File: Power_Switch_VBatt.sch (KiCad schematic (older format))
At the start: 12 parts, among them P5 XT60, Q3 BC817-40, Q4 IPD90P03P4L

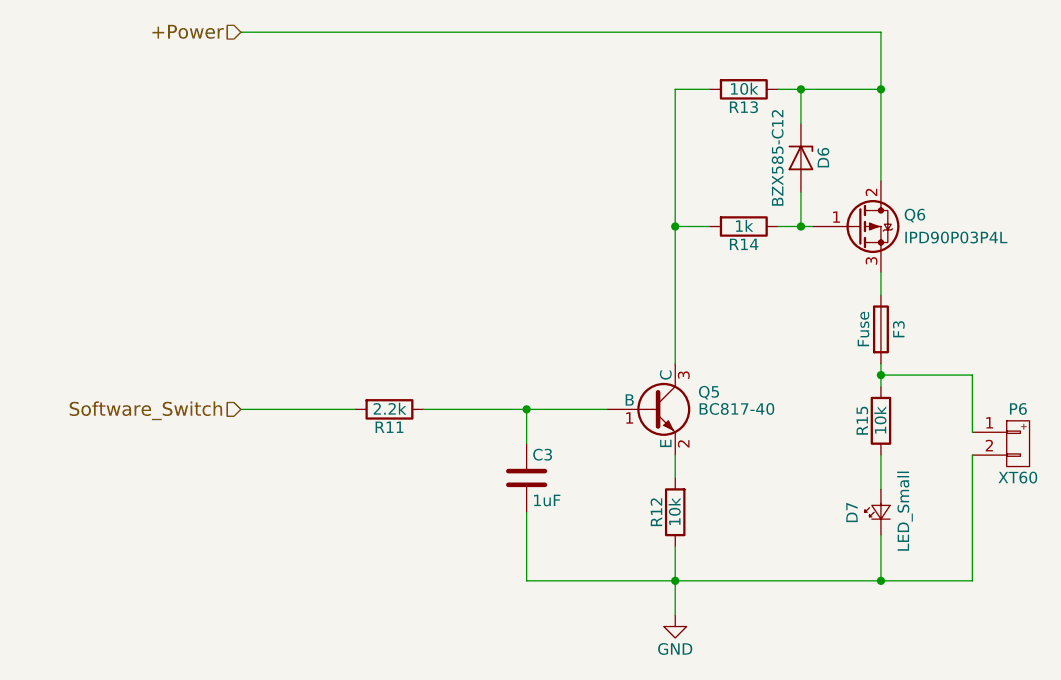
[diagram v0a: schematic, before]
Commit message: Fixed bugs from misunderstanding about Thruster, DVL, and Sonar switch biases.
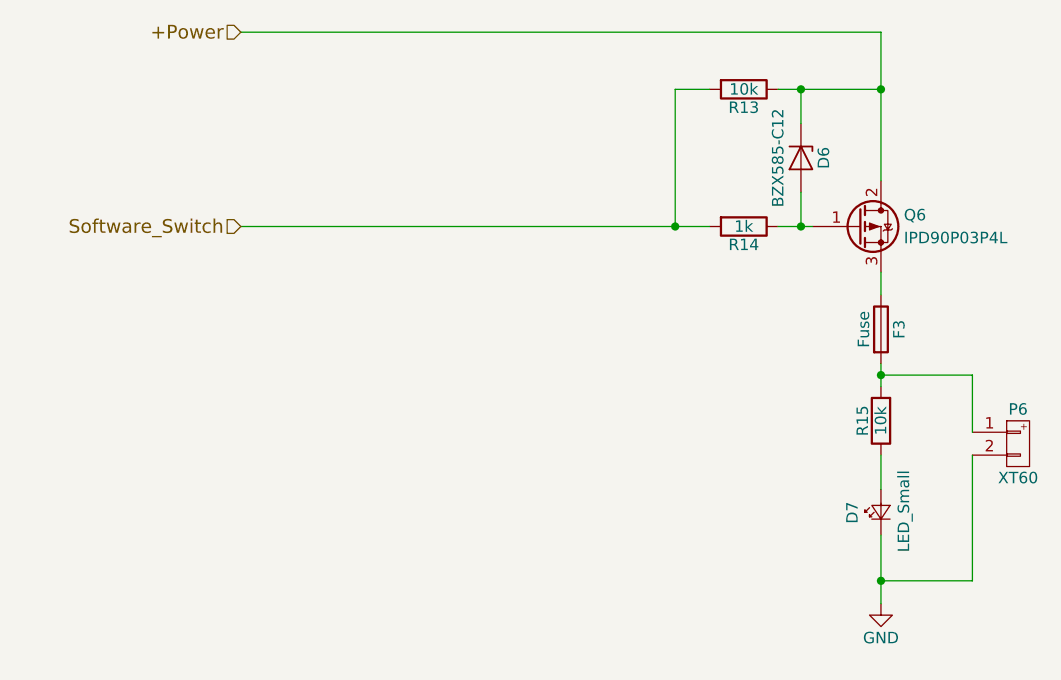
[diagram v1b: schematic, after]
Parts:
- removed C2: 1uF, Capacitors_SMD:C_0603, symbol C
- removed Q3: BC817-40, TO_SOT_Packages_SMD:SOT-23, symbol BC817-40
- removed R6: 2.2k, Resistors_SMD:R_0603, symbol R
- removed R7: 10k, Resistors_SMD:R_0603, symbol R
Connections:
- net Software_Switch: now also R8.2, R9.2
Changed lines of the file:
@@
 encoding utf-8
 Sheet 4 10
-Title ""
+Title "DVL and Sonar Switch"
 Date "2017-04-06"
 Rev "1.0.0"
@@
 $EndComp
 $Comp
-L BC817-40 Q3
-U 1 1 58E52473
-P 5450 4100
-AR Path="/58E51F99/58E52473" Ref="Q3"  Part="1"
-AR Path="/58E527AF/58E52473" Ref="Q5"  Part="1"
-F 0 "Q5" H 5650 4175 50  0000 L CNN
-F 1 "BC817-40" H 5650 4100 50  0000 L CNN
-F 2 "TO_SOT_Packages_SMD:SOT-23" H 5650 4025 50  0001 L CIN
-F 3 "" H 5450 4100 50  0001 L CNN
-	1    5450 4100
-	1    0    0    -1
-$EndComp
-$Comp
-L R R6
-U 1 1 58E526E2
-P 4300 4100
-AR Path="/58E51F99/58E526E2" Ref="R6"  Part="1"
-AR Path="/58E527AF/58E526E2" Ref="R11"  Part="1"
-F 0 "R11" V 4380 4100 50  0000 C CNN
-F 1 "2.2k" V 4300 4100 50  0000 C CNN
-F 2 "Resistors_SMD:R_0603" V 4230 4100 50  0001 C CNN
-F 3 "" H 4300 4100 50  0001 C CNN
-	1    4300 4100
-	0    1    1    0
-$EndComp
-$Comp
-L C C2
-U 1 1 58E5272C
-P 4900 4400
-AR Path="/58E51F99/58E5272C" Ref="C2"  Part="1"
-AR Path="/58E527AF/58E5272C" Ref="C3"  Part="1"
-F 0 "C3" H 4925 4500 50  0000 L CNN
-F 1 "1uF" H 4925 4300 50  0000 L CNN
-F 2 "Capacitors_SMD:C_0603" H 4938 4250 50  0001 C CNN
-F 3 "" H 4900 4400 50  0001 C CNN
-	1    4900 4400
-	1    0    0    -1
-$EndComp
-$Comp
 L GND #PWR017
 U 1 1 58E527F8
-P 5550 5000
+P 6450 4950
 AR Path="/58E51F99/58E527F8" Ref="#PWR017"  Part="1"
 AR Path="/58E527AF/58E527F8" Ref="#PWR018"  Part="1"
-F 0 "#PWR018" H 5550 4750 50  0001 C CNN
-F 1 "GND" H 5550 4850 50  0000 C CNN
-F 2 "" H 5550 5000 50  0001 C CNN
-F 3 "" H 5550 5000 50  0001 C CNN
-	1    5550 5000
+F 0 "#PWR018" H 6450 4700 50  0001 C CNN
+F 1 "GND" H 6450 4800 50  0000 C CNN
+F 2 "" H 6450 4950 50  0001 C CNN
+F 3 "" H 6450 4950 50  0001 C CNN
+	1    6450 4950
 	1    0    0    -1
 $EndComp
 Text HLabel 3650 2450 0    60   Input ~ 0
 +Power
-Text HLabel 3650 4100 0    60   Input ~ 0
+Text HLabel 3650 3300 0    60   Input ~ 0
 Software_Switch
 Wire Wire Line
 	6000 3300 6150 3300
 Wire Wire Line
-	5550 3300 5700 3300
-Wire Wire Line
-	5550 2700 5550 3900
+	3650 3300 5700 3300
 Connection ~ 5550 3300
 Wire Wire Line
-	4450 4100 5250 4100
-Wire Wire Line
-	4900 4100 4900 4250
-Wire Wire Line
-	4900 4550 4900 4850
-Connection ~ 4900 4100
-Wire Wire Line
-	3650 4100 4150 4100
-Wire Wire Line
 	6450 2450 6450 3100
-$Comp
-L R R7
-U 1 1 58E6A1DE
-P 5550 4550
-AR Path="/58E51F99/58E6A1DE" Ref="R7"  Part="1"
-AR Path="/58E527AF/58E6A1DE" Ref="R12"  Part="1"
-F 0 "R12" V 5630 4550 50  0000 C CNN
-F 1 "10k" V 5550 4550 50  0000 C CNN
-F 2 "Resistors_SMD:R_0603" V 5480 4550 50  0001 C CNN
-F 3 "" H 5550 4550 50  0001 C CNN
-	1    5550 4550
-	-1   0    0    1
-$EndComp
-Connection ~ 5550 4850
-Wire Wire Line
-	4900 4850 6850 4850
-Wire Wire Line
-	5550 4300 5550 4400
-Wire Wire Line
-	5550 4700 5550 5000
 $Comp
 L D_Zener D4
@@
 	6450 4300 6450 4450
 Wire Wire Line
-	6450 4850 6450 4650
+	6450 4650 6450 4950
 Wire Wire Line
 	6850 4850 6850 4300
@@
 	6850 3950 6850 4200
 Connection ~ 6450 3950
+Wire Wire Line
+	5550 2700 5550 3300
+Wire Wire Line
+	6850 4850 6450 4850
 $EndSCHEMATC

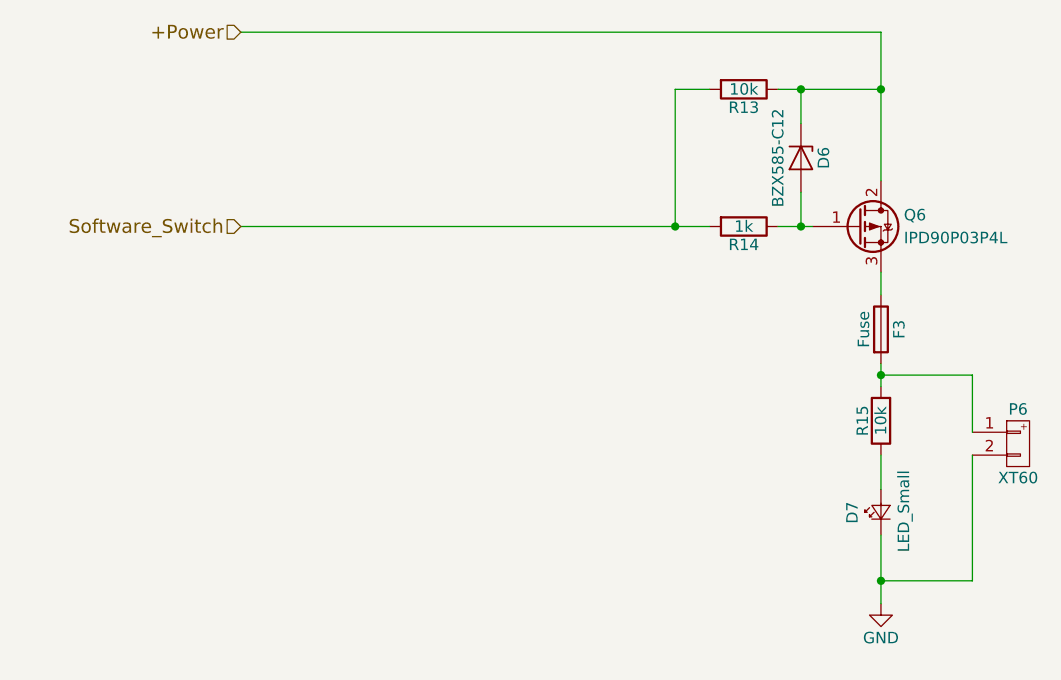
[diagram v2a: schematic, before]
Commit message: update footprint of some LED
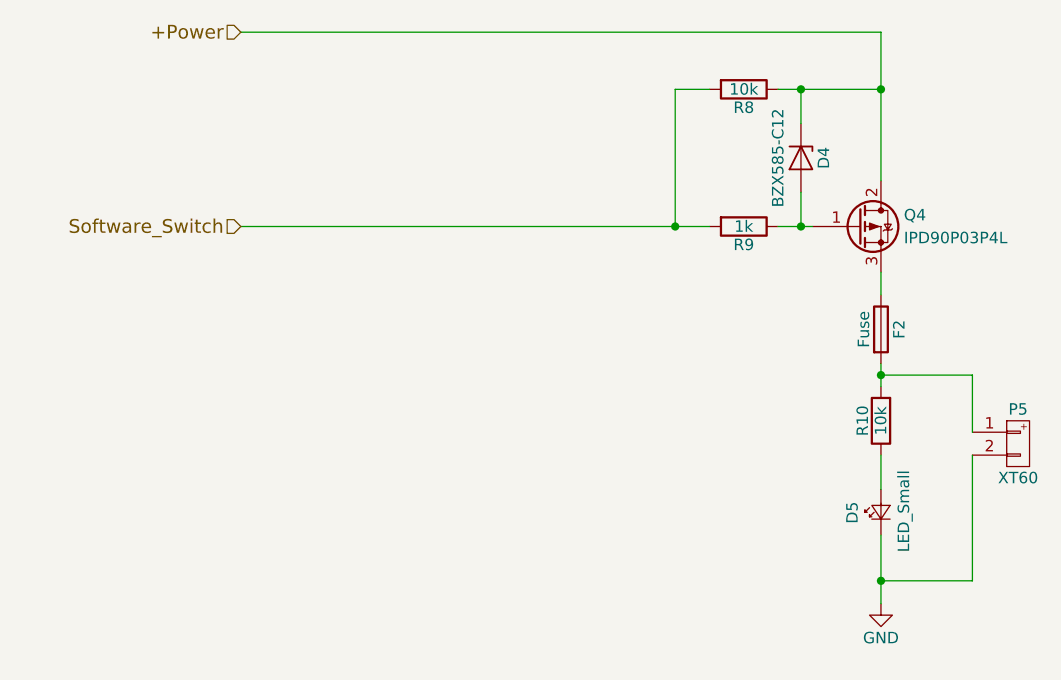
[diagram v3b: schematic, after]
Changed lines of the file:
@@
 $Descr A4 11693 8268
 encoding utf-8
-Sheet 4 10
+Sheet 3 10
 Title "DVL and Sonar Switch"
 Date "2017-04-06"
@@
 AR Path="/58E51F99/58E52089" Ref="Q4"  Part="1"
 AR Path="/58E527AF/58E52089" Ref="Q6"  Part="1"
-F 0 "Q6" H 6550 3350 50  0000 L CNN
+F 0 "Q4" H 6550 3350 50  0000 L CNN
 F 1 "IPD90P03P4L" H 6550 3250 50  0000 L CNN
 F 2 "TO_SOT_Packages_SMD:TO-252-2Lead" H 6550 3400 50  0001 C CNN
@@
 AR Path="/58E51F99/58E5219E" Ref="R9"  Part="1"
 AR Path="/58E527AF/58E5219E" Ref="R14"  Part="1"
-F 0 "R14" V 5930 3300 50  0000 C CNN
+F 0 "R9" V 5930 3300 50  0000 C CNN
 F 1 "1k" V 5850 3300 50  0000 C CNN
 F 2 "Resistors_SMD:R_0603" V 5780 3300 50  0001 C CNN
@@
 AR Path="/58E51F99/58E521F9" Ref="P5"  Part="1"
 AR Path="/58E527AF/58E521F9" Ref="P6"  Part="1"
-F 0 "P6" H 7050 4400 50  0000 C CNN
+F 0 "P5" H 7050 4400 50  0000 C CNN
 F 1 "XT60" H 7050 4100 50  0000 C CNN
 F 2 "zeabus:XT60" H 7150 4000 60  0001 C CNN
@@
 AR Path="/58E51F99/58E52234" Ref="D5"  Part="1"
 AR Path="/58E527AF/58E52234" Ref="D7"  Part="1"
-F 0 "D7" H 6400 4675 50  0000 L CNN
+F 0 "D5" H 6400 4675 50  0000 L CNN
 F 1 "LED_Small" H 6275 4450 50  0000 L CNN
 F 2 "LEDs:LED_0603" V 6450 4550 50  0001 C CNN
@@
 AR Path="/58E51F99/58E5234D" Ref="R8"  Part="1"
 AR Path="/58E527AF/58E5234D" Ref="R13"  Part="1"
-F 0 "R13" V 5930 2700 50  0000 C CNN
+F 0 "R8" V 5930 2700 50  0000 C CNN
 F 1 "10k" V 5850 2700 50  0000 C CNN
 F 2 "Resistors_SMD:R_0603" V 5780 2700 50  0001 C CNN
@@
 AR Path="/58E51F99/58E52389" Ref="R10"  Part="1"
 AR Path="/58E527AF/58E52389" Ref="R15"  Part="1"
-F 0 "R15" V 6530 4150 50  0000 C CNN
+F 0 "R10" V 6530 4150 50  0000 C CNN
 F 1 "10k" V 6450 4150 50  0000 C CNN
 F 2 "Resistors_SMD:R_0603" V 6380 4150 50  0001 C CNN
@@
 $EndComp
 $Comp
-L GND #PWR13
+L GND #PWR013
 U 1 1 58E527F8
 P 6450 4950
-AR Path="/58E51F99/58E527F8" Ref="#PWR13"  Part="1"
-AR Path="/58E527AF/58E527F8" Ref="#PWR14"  Part="1"
-F 0 "#PWR14" H 6450 4700 50  0001 C CNN
+AR Path="/58E51F99/58E527F8" Ref="#PWR013"  Part="1"
+AR Path="/58E527AF/58E527F8" Ref="#PWR014"  Part="1"
+F 0 "#PWR013" H 6450 4700 50  0001 C CNN
 F 1 "GND" H 6450 4800 50  0000 C CNN
 F 2 "" H 6450 4950 50  0001 C CNN
@@
 AR Path="/58E51F99/58E648CE" Ref="D4"  Part="1"
 AR Path="/58E527AF/58E648CE" Ref="D6"  Part="1"
-F 0 "D6" H 6100 3100 50  0000 C CNN
+F 0 "D4" H 6100 3100 50  0000 C CNN
 F 1 "BZX585-C12" H 6100 2900 50  0000 C CNN
 F 2 "Diodes_SMD:SOD-523" H 6100 3000 50  0001 C CNN
@@
 AR Path="/58E51F99/58E651FD" Ref="F2"  Part="1"
 AR Path="/58E527AF/58E651FD" Ref="F3"  Part="1"
-F 0 "F3" V 6530 3750 50  0000 C CNN
+F 0 "F2" V 6530 3750 50  0000 C CNN
 F 1 "Fuse" V 6375 3750 50  0000 C CNN
 F 2 "Zeabus:FUSE_AUTO" V 6380 3750 50  0001 C CNN

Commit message: update footprint of BZX585-C12
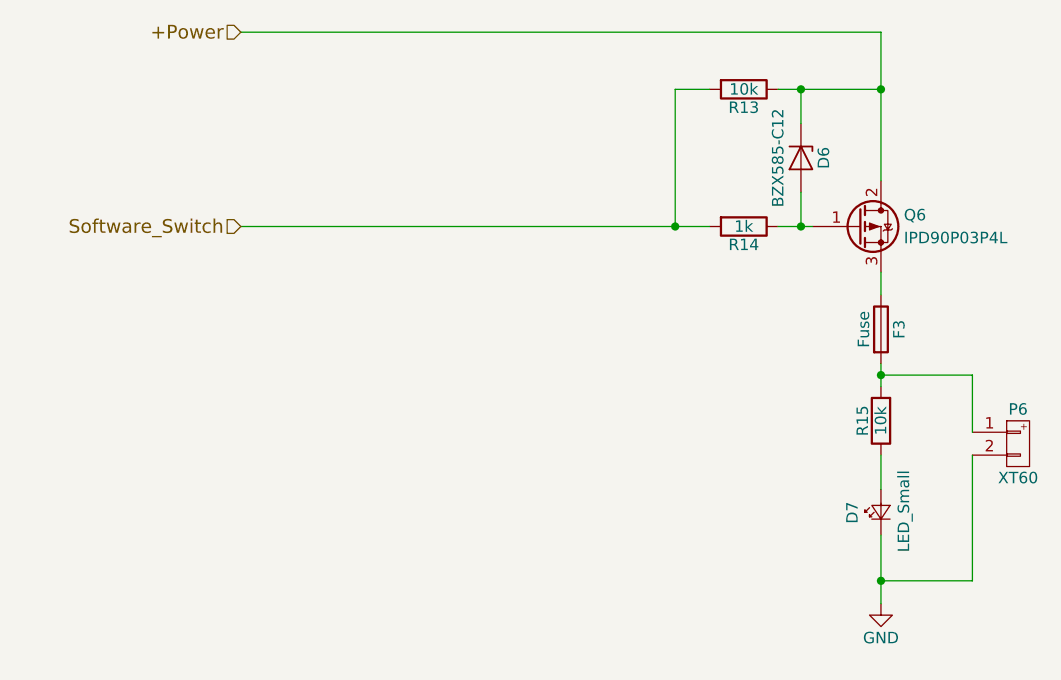
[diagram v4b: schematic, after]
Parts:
- D4: footprint Diodes_SMD:SOD-523 -> Diodes_SMD:D_SOD-523
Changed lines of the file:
@@
 $Descr A4 11693 8268
 encoding utf-8
-Sheet 3 10
+Sheet 4 10
 Title "DVL and Sonar Switch"
 Date "2017-04-06"
@@
 AR Path="/58E51F99/58E52089" Ref="Q4"  Part="1"
 AR Path="/58E527AF/58E52089" Ref="Q6"  Part="1"
-F 0 "Q4" H 6550 3350 50  0000 L CNN
+F 0 "Q6" H 6550 3350 50  0000 L CNN
 F 1 "IPD90P03P4L" H 6550 3250 50  0000 L CNN
 F 2 "TO_SOT_Packages_SMD:TO-252-2Lead" H 6550 3400 50  0001 C CNN
@@
 AR Path="/58E51F99/58E5219E" Ref="R9"  Part="1"
 AR Path="/58E527AF/58E5219E" Ref="R14"  Part="1"
-F 0 "R9" V 5930 3300 50  0000 C CNN
+F 0 "R14" V 5930 3300 50  0000 C CNN
 F 1 "1k" V 5850 3300 50  0000 C CNN
 F 2 "Resistors_SMD:R_0603" V 5780 3300 50  0001 C CNN
@@
 AR Path="/58E51F99/58E521F9" Ref="P5"  Part="1"
 AR Path="/58E527AF/58E521F9" Ref="P6"  Part="1"
-F 0 "P5" H 7050 4400 50  0000 C CNN
+F 0 "P6" H 7050 4400 50  0000 C CNN
 F 1 "XT60" H 7050 4100 50  0000 C CNN
 F 2 "zeabus:XT60" H 7150 4000 60  0001 C CNN
@@
 AR Path="/58E51F99/58E52234" Ref="D5"  Part="1"
 AR Path="/58E527AF/58E52234" Ref="D7"  Part="1"
-F 0 "D5" H 6400 4675 50  0000 L CNN
+F 0 "D7" H 6400 4675 50  0000 L CNN
 F 1 "LED_Small" H 6275 4450 50  0000 L CNN
 F 2 "LEDs:LED_0603" V 6450 4550 50  0001 C CNN
@@
 AR Path="/58E51F99/58E5234D" Ref="R8"  Part="1"
 AR Path="/58E527AF/58E5234D" Ref="R13"  Part="1"
-F 0 "R8" V 5930 2700 50  0000 C CNN
+F 0 "R13" V 5930 2700 50  0000 C CNN
 F 1 "10k" V 5850 2700 50  0000 C CNN
 F 2 "Resistors_SMD:R_0603" V 5780 2700 50  0001 C CNN
@@
 AR Path="/58E51F99/58E52389" Ref="R10"  Part="1"
 AR Path="/58E527AF/58E52389" Ref="R15"  Part="1"
-F 0 "R10" V 6530 4150 50  0000 C CNN
+F 0 "R15" V 6530 4150 50  0000 C CNN
 F 1 "10k" V 6450 4150 50  0000 C CNN
 F 2 "Resistors_SMD:R_0603" V 6380 4150 50  0001 C CNN
@@
 AR Path="/58E51F99/58E527F8" Ref="#PWR013"  Part="1"
 AR Path="/58E527AF/58E527F8" Ref="#PWR014"  Part="1"
-F 0 "#PWR013" H 6450 4700 50  0001 C CNN
+F 0 "#PWR014" H 6450 4700 50  0001 C CNN
 F 1 "GND" H 6450 4800 50  0000 C CNN
 F 2 "" H 6450 4950 50  0001 C CNN
@@
 AR Path="/58E51F99/58E648CE" Ref="D4"  Part="1"
 AR Path="/58E527AF/58E648CE" Ref="D6"  Part="1"
-F 0 "D4" H 6100 3100 50  0000 C CNN
+F 0 "D6" H 6100 3100 50  0000 C CNN
 F 1 "BZX585-C12" H 6100 2900 50  0000 C CNN
-F 2 "Diodes_SMD:SOD-523" H 6100 3000 50  0001 C CNN
+F 2 "Diodes_SMD:D_SOD-523" H 6100 3000 50  0001 C CNN
 F 3 "" H 6100 3000 50  0001 C CNN
 	1    6100 3000
@@
 AR Path="/58E51F99/58E651FD" Ref="F2"  Part="1"
 AR Path="/58E527AF/58E651FD" Ref="F3"  Part="1"
-F 0 "F2" V 6530 3750 50  0000 C CNN
+F 0 "F3" V 6530 3750 50  0000 C CNN
 F 1 "Fuse" V 6375 3750 50  0000 C CNN
 F 2 "Zeabus:FUSE_AUTO" V 6380 3750 50  0001 C CNN

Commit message: Update Netlist
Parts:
- renumbered D4 to D3, D5 to D4, Q4 to Q2, R8 to R4, R9 to R5, R10 to R6
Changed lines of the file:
@@
 $EndDescr
 $Comp
-L Q_PMOS_GDS Q4
+L Q_PMOS_GDS Q2
 U 1 1 58E52089
 P 6350 3300
-AR Path="/58E51F99/58E52089" Ref="Q4"  Part="1"
-AR Path="/58E527AF/58E52089" Ref="Q6"  Part="1"
-F 0 "Q6" H 6550 3350 50  0000 L CNN
+AR Path="/58E51F99/58E52089" Ref="Q2"  Part="1"
+AR Path="/58E527AF/58E52089" Ref="Q3"  Part="1"
+F 0 "Q3" H 6550 3350 50  0000 L CNN
 F 1 "IPD90P03P4L" H 6550 3250 50  0000 L CNN
 F 2 "TO_SOT_Packages_SMD:TO-252-2Lead" H 6550 3400 50  0001 C CNN
@@
 $EndComp
 $Comp
-L R R9
+L R R5
 U 1 1 58E5219E
 P 5850 3300
-AR Path="/58E51F99/58E5219E" Ref="R9"  Part="1"
-AR Path="/58E527AF/58E5219E" Ref="R14"  Part="1"
-F 0 "R14" V 5930 3300 50  0000 C CNN
+AR Path="/58E51F99/58E5219E" Ref="R5"  Part="1"
+AR Path="/58E527AF/58E5219E" Ref="R8"  Part="1"
+F 0 "R8" V 5930 3300 50  0000 C CNN
 F 1 "1k" V 5850 3300 50  0000 C CNN
 F 2 "Resistors_SMD:R_0603" V 5780 3300 50  0001 C CNN
@@
 $EndComp
 $Comp
-L LED_Small D5
+L LED_Small D4
 U 1 1 58E52234
 P 6450 4550
-AR Path="/58E51F99/58E52234" Ref="D5"  Part="1"
-AR Path="/58E527AF/58E52234" Ref="D7"  Part="1"
-F 0 "D7" H 6400 4675 50  0000 L CNN
+AR Path="/58E51F99/58E52234" Ref="D4"  Part="1"
+AR Path="/58E527AF/58E52234" Ref="D6"  Part="1"
+F 0 "D6" H 6400 4675 50  0000 L CNN
 F 1 "LED_Small" H 6275 4450 50  0000 L CNN
 F 2 "LEDs:LED_0603" V 6450 4550 50  0001 C CNN
@@
 $EndComp
 $Comp
-L R R8
+L R R4
 U 1 1 58E5234D
 P 5850 2700
-AR Path="/58E51F99/58E5234D" Ref="R8"  Part="1"
-AR Path="/58E527AF/58E5234D" Ref="R13"  Part="1"
-F 0 "R13" V 5930 2700 50  0000 C CNN
+AR Path="/58E51F99/58E5234D" Ref="R4"  Part="1"
+AR Path="/58E527AF/58E5234D" Ref="R7"  Part="1"
+F 0 "R7" V 5930 2700 50  0000 C CNN
 F 1 "10k" V 5850 2700 50  0000 C CNN
 F 2 "Resistors_SMD:R_0603" V 5780 2700 50  0001 C CNN
@@
 $EndComp
 $Comp
-L R R10
+L R R6
 U 1 1 58E52389
 P 6450 4150
-AR Path="/58E51F99/58E52389" Ref="R10"  Part="1"
-AR Path="/58E527AF/58E52389" Ref="R15"  Part="1"
-F 0 "R15" V 6530 4150 50  0000 C CNN
+AR Path="/58E51F99/58E52389" Ref="R6"  Part="1"
+AR Path="/58E527AF/58E52389" Ref="R9"  Part="1"
+F 0 "R9" V 6530 4150 50  0000 C CNN
 F 1 "10k" V 6450 4150 50  0000 C CNN
 F 2 "Resistors_SMD:R_0603" V 6380 4150 50  0001 C CNN
@@
 $EndComp
 $Comp
-L GND #PWR013
+L GND #PWR13
 U 1 1 58E527F8
 P 6450 4950
-AR Path="/58E51F99/58E527F8" Ref="#PWR013"  Part="1"
-AR Path="/58E527AF/58E527F8" Ref="#PWR014"  Part="1"
-F 0 "#PWR014" H 6450 4700 50  0001 C CNN
+AR Path="/58E51F99/58E527F8" Ref="#PWR13"  Part="1"
+AR Path="/58E527AF/58E527F8" Ref="#PWR14"  Part="1"
+F 0 "#PWR14" H 6450 4700 50  0001 C CNN
 F 1 "GND" H 6450 4800 50  0000 C CNN
 F 2 "" H 6450 4950 50  0001 C CNN
@@
 	6450 2450 6450 3100
 $Comp
-L D_Zener D4
+L D_Zener D3
 U 1 1 58E648CE
 P 6100 3000
-AR Path="/58E51F99/58E648CE" Ref="D4"  Part="1"
-AR Path="/58E527AF/58E648CE" Ref="D6"  Part="1"
-F 0 "D6" H 6100 3100 50  0000 C CNN
+AR Path="/58E51F99/58E648CE" Ref="D3"  Part="1"
+AR Path="/58E527AF/58E648CE" Ref="D5"  Part="1"
+F 0 "D5" H 6100 3100 50  0000 C CNN
 F 1 "BZX585-C12" H 6100 2900 50  0000 C CNN
 F 2 "Diodes_SMD:D_SOD-523" H 6100 3000 50  0001 C CNN
